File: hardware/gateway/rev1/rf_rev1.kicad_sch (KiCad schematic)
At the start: 28 parts, among them IC2 CC1101RGPR, Y1 NX3225GA-26.000M-STD-CRG-2

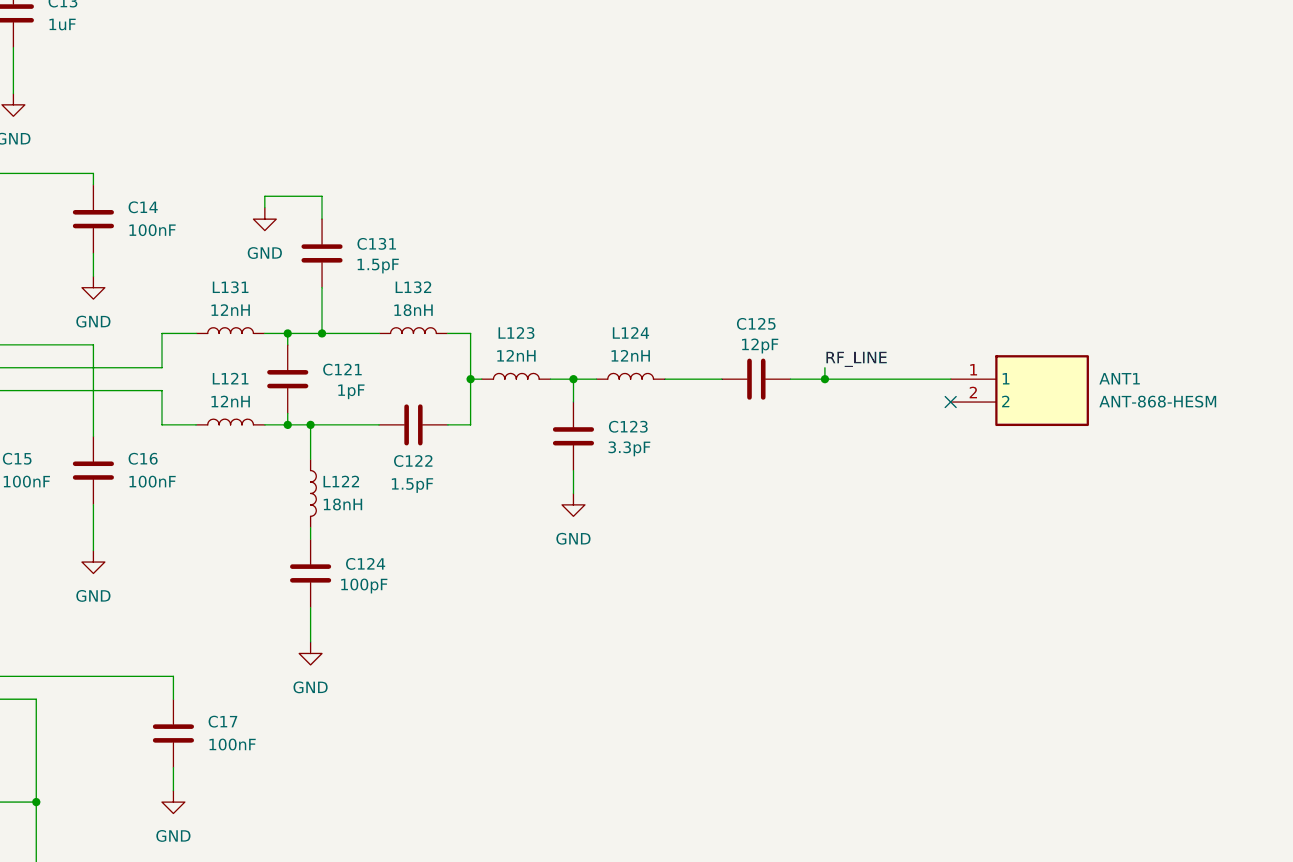
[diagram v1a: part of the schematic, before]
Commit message: Schematic adapted for 433 MHz.
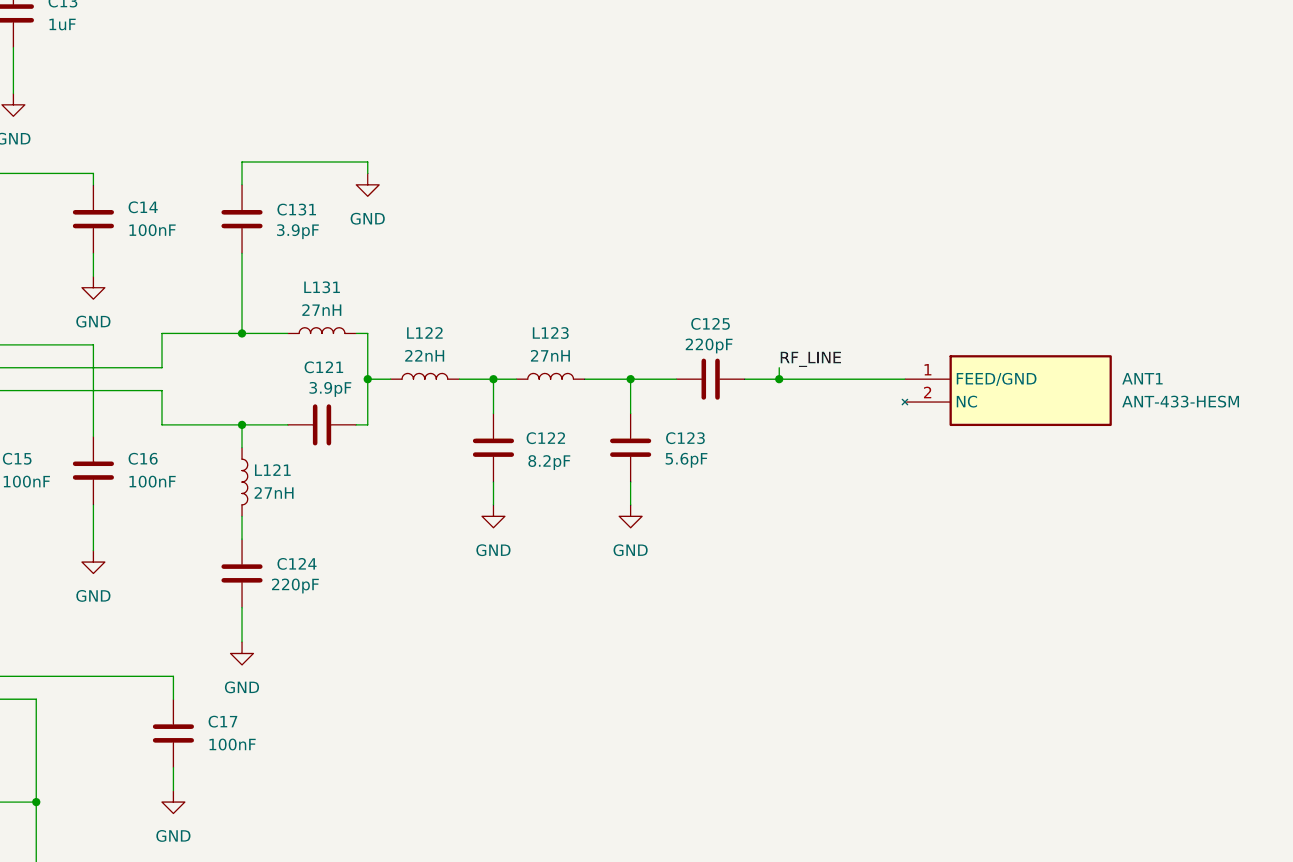
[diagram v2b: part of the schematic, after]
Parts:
- removed ANT1: ANT-868-HESM, MyParts:ANT-868-HESM, symbol ANT-868-HESM:ANT-868-HESM
- removed L124: 12nH, Inductor_SMD:L_0402_1005Metric, symbol Device:L
- removed L132: 18nH, Inductor_SMD:L_0402_1005Metric, symbol Device:L
- added ANT1: ANT-433-HESM, MyParts:ANT433HESM, symbol ANT-433-HESM:ANT-433-HESM
- C121: value 1pF -> 3.9pF; Manufacturer Part Number GRM1555C1H1R0BA01J -> GRM1555C1E3R9CA1D; Mouser Part Number 81-GRM1555C1H1R0BA1J -> 81-GRM1555C1E3R9CA1D; Supplier Link https://pt.mouser.com/ProductDetail/Murata-Electronics/GRM1555C1H1R0BA01J?qs=ouTquLLW2S5DcHZ7kLUjdg%3D%3D -> https://pt.mouser.com/ProductDetail/Murata-Electronics/GRM1555C1E3R9CA01D?qs=ouTquLLW2S6No2iW5vpMPQ%3D%3D
- C122: value 1.5pF -> 8.2pF; Manufacturer Part Number GRM1555C1E1R5BA01D -> GCQ0335C1H8R2WB1D; Mouser Part Number 81-GRM1555C1E1R5BA1D -> 81-GCQ0335C1H8R2WB1D; Supplier Link https://pt.mouser.com/ProductDetail/Murata-Electronics/GRM1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 -> https://pt.mouser.com/ProductDetail/Murata-Electronics/GCQ0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
- C123: value 3.3pF -> 5.6pF; Manufacturer Part Number GRM1555C1H3R3WA01D -> GCQ0335C1H5R6BB1D; Mouser Part Number 81-GRM1555C1H3R3WA1D -> 81-GCQ0335C1H5R6BB1D; Supplier Link https://pt.mouser.com/ProductDetail/Murata-Electronics/GRM1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 -> https://pt.mouser.com/ProductDetail/Murata-Electronics/GCQ0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
- C124: value 100pF -> 220pF; Manufacturer Part Number GRM1555C1H101FA01J -> GRM0225C1C221JA2L; Mouser Part Number 81-GRM1555C1H101FA1J -> 81-GRM0225C1C221JA2L; Supplier Link https://pt.mouser.com/ProductDetail/Murata-Electronics/GRM1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 -> https://pt.mouser.com/ProductDetail/Murata-Electronics/GRM0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
- C125: value 12pF -> 220pF; Manufacturer Part Number GRM1555C1H120FA01D -> GRM0225C1C221JA2L; Mouser Part Number 81-GRM1555C1H120FA1D -> 81-GRM0225C1C221JA2L; Supplier Link https://pt.mouser.com/ProductDetail/Murata-Electronics/GRM1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 -> https://pt.mouser.com/ProductDetail/Murata-Electronics/GRM0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
- C131: value 1.5pF -> 3.9pF; Manufacturer Part Number GRM1555C1E1R5BA01D -> GRM1555C1E3R9CA1D; Mouser Part Number 81-GRM1555C1E1R5BA1D -> 81-GRM1555C1E3R9CA1D; Supplier Link https://pt.mouser.com/ProductDetail/Murata-Electronics/GRM1555C1E1R5BA01D?qs=ouTquLLW2S6xHAnxxZWZ1w%3D%3D -> https://pt.mouser.com/ProductDetail/Murata-Electronics/GRM1555C1E3R9CA01D?qs=ouTquLLW2S6No2iW5vpMPQ%3D%3D
- L121, L123, L131: value 12nH -> 27nH; Manufacturer Part Number LQW15AN12NJ80D -> LQG15HS27NJ02D; Mouser Part Number 81-LQW15AN12NJ80D -> 81-LQG15HS27NJ02D; Supplier Link https://pt.mouser.com/ProductDetail/Murata-Electronics/LQW1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 -> https://pt.mouser.com/ProductDetail/Murata-Electronics/LQG1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
- L122: value 18nH -> 22nH; Manufacturer Part Number LQG15HH18NJ02D -> LQW15CA22NJ00D; Mouser Part Number 81-LQG15HH18NJ02D -> 81-LQW15CA22NJ00D; Supplier Link https://pt.mouser.com/ProductDetail/Murata-Electronics/LQG1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 -> https://pt.mouser.com/ProductDetail/Murata-Electronics/LQW1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
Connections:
- net GND: now also C122.1
- net RF_LINE: now also ANT1.1 (FEED/GND)
- net at IC2.13 (RF_N), L131.1: now also C131.1
- net at C121.1, L122.1: now also L131.2; no longer C122.1, L121.2
- net at C125.1: now also C123.2, L123.2
- net at IC2.12 (RF_P), L121.1: now also C121.2
- net at C124.2: now also L121.2; no longer L122.2
- net at C122.2, L123.1: now also L122.2
- no-connect marks 2 -> 1
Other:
- moved on the sheet: C121, C122, C123, C124, C125, C131, L121, L122, L123, L131

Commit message: DRC errors fixed and silkscreen fixed.
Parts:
- renumbered C131 to C20, C124 to C21, C121 to C22, C122 to C23, C123 to C24, C125 to C25, L131 to L1, L121 to L2, L122 to L3, L123 to L4
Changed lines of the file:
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@@
 		(dnp no)
 		(fields_autoplaced yes)
-		(property "Reference" "L131"
+		(property "Reference" "L1"
 			(at 165.1 71.12 90)
 			(effects
@@
 			(project "gateway_rev1"
 				(path "/d3cb7130-decc-418b-958e-e5d84a8d867f/af07603d-259f-481d-be2c-d925e27835a3"
-					(reference "L131")
+					(reference "L1")
 					(unit 1)
 				)
@@
 		(on_board yes)
 		(dnp no)
-		(property "Reference" "C121"
+		(property "Reference" "C22"
 			(at 163.068 80.01 90)
 			(effects
@@
 			(project "gateway_rev1"
 				(path "/d3cb7130-decc-418b-958e-e5d84a8d867f/af07603d-259f-481d-be2c-d925e27835a3"
-					(reference "C121")
+					(reference "C22")
 					(unit 1)
 				)
@@
 		(on_board yes)
 		(dnp no)
-		(property "Reference" "C125"
+		(property "Reference" "C25"
 			(at 210.566 75.184 90)
 			(effects
@@
 			(project "gateway_rev1"
 				(path "/d3cb7130-decc-418b-958e-e5d84a8d867f/af07603d-259f-481d-be2c-d925e27835a3"
-					(reference "C125")
+					(reference "C25")
 					(unit 1)
 				)
@@
 		(on_board yes)
 		(dnp no)
-		(property "Reference" "C131"
+		(property "Reference" "C20"
 			(at 164.592 62.484 0)
 			(effects
@@
 			(project "gateway_rev1"
 				(path "/d3cb7130-decc-418b-958e-e5d84a8d867f/af07603d-259f-481d-be2c-d925e27835a3"
-					(reference "C131")
+					(reference "C20")
 					(unit 1)
 				)
@@
 		(dnp no)
 		(fields_autoplaced yes)
-		(property "Reference" "L121"
+		(property "Reference" "L2"
 			(at 157.48 91.4399 0)
 			(effects
@@
 			(project "gateway_rev1"
 				(path "/d3cb7130-decc-418b-958e-e5d84a8d867f/af07603d-259f-481d-be2c-d925e27835a3"
-					(reference "L121")
+					(reference "L2")
 					(unit 1)
 				)
@@
 		(on_board yes)
 		(dnp no)
-		(property "Reference" "C124"
+		(property "Reference" "C21"
 			(at 164.592 101.854 0)
 			(effects
@@
 			(project "gateway_rev1"
 				(path "/d3cb7130-decc-418b-958e-e5d84a8d867f/af07603d-259f-481d-be2c-d925e27835a3"
-					(reference "C124")
+					(reference "C21")
 					(unit 1)
 				)
@@
 		(dnp no)
 		(fields_autoplaced yes)
-		(property "Reference" "L123"
+		(property "Reference" "L4"
 			(at 190.5 76.2 90)
 			(effects
@@
 			(project "gateway_rev1"
 				(path "/d3cb7130-decc-418b-958e-e5d84a8d867f/af07603d-259f-481d-be2c-d925e27835a3"
-					(reference "L123")
+					(reference "L4")
 					(unit 1)
 				)
@@
 		(dnp no)
 		(fields_autoplaced yes)
-		(property "Reference" "L122"
+		(property "Reference" "L3"
 			(at 176.53 76.2 90)
 			(effects
@@
 			(project "gateway_rev1"
 				(path "/d3cb7130-decc-418b-958e-e5d84a8d867f/af07603d-259f-481d-be2c-d925e27835a3"
-					(reference "L122")
+					(reference "L3")
 					(unit 1)
 				)
@@
 		(on_board yes)
 		(dnp no)
-		(property "Reference" "C123"
+		(property "Reference" "C24"
 			(at 207.772 87.884 0)
 			(effects
@@
 			(project "gateway_rev1"
 				(path "/d3cb7130-decc-418b-958e-e5d84a8d867f/af07603d-259f-481d-be2c-d925e27835a3"
-					(reference "C123")
+					(reference "C24")
 					(unit 1)
 				)
@@
 		(on_board yes)
 		(dnp no)
-		(property "Reference" "C122"
+		(property "Reference" "C23"
 			(at 192.278 87.884 0)
 			(effects
@@
 			(project "gateway_rev1"
 				(path "/d3cb7130-decc-418b-958e-e5d84a8d867f/af07603d-259f-481d-be2c-d925e27835a3"
-					(reference "C122")
+					(reference "C23")
 					(unit 1)
 				)

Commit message: BOM fixed and finance updated
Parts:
- ANT1: Manufacturer Name (none) -> TE Connectivity; Manufacturer Part Number (none) -> ANT-433-HESM; Manufacturer_Name TE Connectivity -> (none); Manufacturer_Part_Number ANT-433-HESM -> (none); Mouser Price/Stock https://www.mouser.co.uk/ProductDetail/Linx-Technologies/AN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 -> (none); Supplier Link (none) -> https://www.mouser.co.uk/ProductDetail/Linx-Technologies/AN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
- C23: Manufacturer Part Number GCQ0335C1H8R2WB1D -> GQM1555C2D8R2WB1D; Mouser Part Number 81-GCQ0335C1H8R2WB1D -> 81-GQM1555C2D8R2WB1D; Supplier Link https://pt.mouser.com/ProductDetail/Murata-Electronics/GCQ0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 -> https://pt.mouser.com/ProductDetail/Murata-Electronics/GQM1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
- C24: Manufacturer Part Number GCQ0335C1H5R6BB1D -> GCQ1555C1H5R6WB1D; Mouser Part Number 81-GCQ0335C1H5R6BB1D -> 81-GCQ1555C1H5R6WB1D; Supplier Link https://pt.mouser.com/ProductDetail/Murata-Electronics/GCQ0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 -> https://pt.mouser.com/ProductDetail/Murata-Electronics/GCQ1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
- C9: Manufacturer Part Number JMK325B7476MM-PR -> JMK316BJ476MD-T; Mouser Part Number 963-JMK325B7476MM-PR -> 963-JMK316BJ476MD-T; Supplier Link https://pt.mouser.com/ProductDetail/TAIYO-YUDEN/JMK325B7476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 -> https://pt.mouser.com/ProductDetail/TAIYO-YUDEN/JMK316BJ476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
